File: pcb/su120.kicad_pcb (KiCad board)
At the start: 2 copper layers, 98.8 x 98 mm, 343 parts, among them J1 MJ-4PP-9, J2 Conn_01x03, J3 Conn_01x08, J4 Conn_01x08, J5 Conn_01x03, J6 MJ-4PP-9, J7 Conn_02x05_Odd_Even, J8 Conn_02x05_Odd_Even, SW1 SW_Push, SW10 SW_Push, SW11 SW_Push, SW12 SW_Push, SW13 SW_Push, SW14 SW_Push, SW15 SW_Push, SW16 SW_Push, SW17 SW_Push, SW18 SW_Push, SW19 Rotary_Encoder_Switch, SW2 SW_Push, SW20 Rotary_Encoder_Switch, SW21 SW_Push, SW3 SW_Push, SW4 SW_Push, SW5 SW_Push, SW6 SW_Push, SW7 SW_Push, SW8 SW_Push, SW9 SW_Push, U1 ProMicro

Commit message: first
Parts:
- removed the ? at (77.8, 59.5)
- removed the ? at (39.3, 150.4)
- removed the ? at (47.2, 150.4)
- removed the ? at (47.2, 142.1)
- removed the ? at (63.5, 135.7)
- removed the ? at (73.0, 135.7)
- removed the ? at (87.3, 135.7)
- removed the ? at (96.8, 135.7)
- removed the ? at (101.6, 135.7)
- removed the ? at (115.9, 135.7)
- removed the ? at (120.7, 135.7)
- removed the ? at (134.9, 135.7)
- removed the ? at (134.9, 150.0)
- removed the ? at (47.2, 145.7)
- removed the ? at (120.7, 150.0)
- removed the ? at (115.9, 150.0)
- removed the ? at (101.6, 150.0)
- removed the ? at (96.8, 150.0)
- removed the ? at (87.3, 150.0)
- removed the ? at (73.0, 150.0)
- removed the ? at (63.5, 150.0)
- removed the ? at (43.3, 142.1)
- removed the ? at (43.3, 135.3)
- removed the ? at (130.0, 55.2)
- removed the ? at (47.2, 135.3)
- removed the ? at (135.3, 55.2)
- removed the ? at (91.7, 55.2)
- removed the ? at (86.4, 55.2)
- removed the ? at (121.3, 55.2)
- removed the ? at (112.5, 55.2)
- removed the ? at (117.9, 55.2)
- removed the ? at (126.6, 55.2)
- removed the ? at (95.1, 55.2)
- removed the ? at (100.4, 55.2)
- removed the ? at (109.1, 55.2)
- removed the ? at (51.2, 142.1)
- removed the ? at (103.8, 55.2)
- removed the ? at (43.3, 150.4)
- removed the ? at (43.3, 145.7)
- removed the ? at (78.6, 66.7)
- removed the ? at (80.2, 59.5)
- removed the ? at (61.1, 152.4)
- removed the ? at (137.3, 57.2)
- removed the ? at (61.1, 133.3)
- removed the ? at (99.2, 152.4)
- removed the ? at (118.3, 152.4)
- removed the ? at (51.2, 145.7)
- removed the ? at (137.3, 152.4)
- removed the ? at (137.3, 133.3)
- removed the ? at (137.3, 114.3)
- removed the ? at (137.3, 95.2)
- removed the ? at (137.3, 76.2)
- removed the ? at (99.2, 76.2)
- removed the ? at (99.2, 133.4)
- removed the ? at (118.3, 133.4)
- removed the ? at (51.2, 135.3)
- removed the ? at (118.3, 76.2)
- removed the ? at (80.2, 73.8)
- removed the ? at (90.5, 143.3)
- removed the ? at (127.8, 142.9)
- removed the ? at (51.2, 150.4)
- removed the ? at (108.7, 142.9)
- removed the ? at (80.2, 142.9) (x2)
- removed the ? at (55.2, 142.1)
- removed the ? at (70.2, 143.3)
- removed the ? at (123.0, 66.7)
- removed the ? at (104.0, 66.7)
- removed the ? at (82.5, 59.5)
- removed the ? at (55.2, 145.7)
- removed the ? at (108.7, 63.5)
- removed the ? at (127.8, 63.5)
- removed the ? at (55.2, 135.3)
- removed the ? at (55.2, 150.4)
- removed the ? at (59.1, 135.4)
- removed the ? at (59.1, 150.4)
- removed the ? at (40.1, 80.2)
- removed the ? at (40.1, 75.4)
- removed the ? at (40.1, 84.9)
- removed the ? at (40.1, 70.6)
- removed the ? at (40.1, 88.5)
- removed the ? at (82.5, 73.8)
- removed the ? at (40.1, 98.0)
- removed the ? at (40.1, 102.8)
- removed the ? at (40.1, 93.3)
- removed the ? at (56.0, 55.2)
- removed the ? at (59.9, 55.2)
- removed the ? at (66.7, 55.2)
- removed the ? at (40.1, 106.4)
- removed the ? at (40.1, 111.1)
- removed the ? at (40.1, 120.7)
- removed the ? at (40.1, 115.9)
- removed the ? at (77.8, 73.8)
- removed the ? at (40.1, 131.4)
- removed the ? at (40.1, 124.2)
- removed the ? at (39.3, 142.5)
- removed the ? at (39.3, 135.3)
- removed the ? at (70.1, 55.2)
- removed the ? at (82.9, 55.2)
- removed the ? at (74.4, 55.2)
- removed the ? at (40.1, 58.5)
- removed the ? at (40.1, 67.1)
- removed the ? at (42.9, 55.2)
- removed the ? at (52.4, 55.2)
- removed the ? at (47.6, 55.2)
- removed the ? at (59.1, 141.8)
- removed the ? at (39.3, 145.7)
- removed D16, D17, D18, D19, D20: D, #footprint:diode_TH_SMD_rev2
- removed H133, H134, H135, H136, H137, H138, H139, H140, H210, H211, H212, H213, H41, H42, H43, H44, H45, H46, H47, H48, H49, H50, H57: MountingHole_Pad, #footprint:1pin_conn
- removed J1, J6: MJ-4PP-9, #footprint:MJ-4PP-9
- removed J2, J5: Conn_01x03, #footprint:StripLED_rev2
- removed J3, J4: Conn_01x08, #footprint:PinHeader_1x08_P2.54mm_Vertical_rev2
- removed J7, J8: Conn_02x05_Odd_Even, #footprint:IDC-Header_2x05_P2.54mm_Vertical
- removed JP1, JP2, JP3, JP4, JP5, JP6: SolderJumper_2_Open, #footprint:SolderJumper-2_P1.3mm_Open_Pad1.0x1.0mm
- removed SW16, SW17, SW21: SW_Push, #footprint:CherryMX_MidHeight_Choc_Hotswap_rev5
- removed SW18: SW_Push, #footprint:ResetSW
- removed SW19, SW20: Rotary_Encoder_Switch, #footprint:RotaryEncoder_Alps_EC11E-Switch_Vertical_H20mm_rev2
- removed U1: ProMicro, #footprint:ArduinoProMicro-ZigZag_rev5
- added ?: , #footprint:M1.4_tapping_Hole_rev2, F.Cu at (101.6, 40.5)
- added ?: , #footprint:M1.4_tapping_Hole_rev2, F.Cu at (120.7, 54.8)
- added ?: , #footprint:M1.4_tapping_Hole_rev2, F.Cu at (58.7, 54.8)
- added ?: , #footprint:M1.4_tapping_Hole_rev2, F.Cu at (134.9, 54.8)
- added ?: , #footprint:M1.4_tapping_Hole_rev2, F.Cu at (134.9, 40.5)
- added ?: , #footprint:M1.4_tapping_Hole_rev2, F.Cu at (96.8, 54.8)
- added ?: , #footprint:M1.4_tapping_Hole_rev2, F.Cu at (101.6, 54.8)
- added ?: , #footprint:M1.4_tapping_Hole_rev2, F.Cu at (58.7, 40.5)
- added ?: , #footprint:M2_Hole, F.Cu at (118.3, 76.2)
- added ?: , #footprint:M1.4_tapping_Hole_rev2, F.Cu at (44.5, 54.8)
- added ?: , #footprint:M2_Hole, F.Cu at (61.1, 57.2)
- added ?: , #footprint:M1.4_tapping_Hole_rev2, F.Cu at (77.8, 54.8)
- added ?: , #footprint:M1.4_tapping_Hole_rev2, F.Cu at (63.5, 73.8)
- added ?: , #footprint:M1.4_tapping_Hole_rev2, F.Cu at (77.8, 73.8)
- added ?: , #footprint:M1.4_tapping_Hole_rev2, F.Cu at (63.5, 54.8)
- added ?: , #footprint:M2_Hole, F.Cu at (61.1, 76.2)
- added ?: , #footprint:M1.4_tapping_Hole_rev2, F.Cu at (63.5, 40.5)
- added ?: , #footprint:M1.4_tapping_Hole_rev2, F.Cu at (82.5, 73.8)
- added ?: , #footprint:M2_Hole, F.Cu at (118.3, 57.2)
- added ?: , #footprint:M1.4_tapping_Hole_rev2, F.Cu at (115.9, 40.5)
- added ?: , #footprint:M1.4_tapping_Hole_rev2, F.Cu at (77.8, 59.5)
- added ?: , #footprint:M1.4_tapping_Hole_rev2, F.Cu at (63.5, 59.5)
- added ?: , #footprint:M2_Hole, F.Cu at (80.2, 57.2)
- added ?: , #footprint:M2_Hole, F.Cu at (99.2, 76.2)
- added ?: , #footprint:M1.4_tapping_Hole_rev2, F.Cu at (77.8, 40.5)
- added ?: , #footprint:M1.4_tapping_Hole_rev2, F.Cu at (58.7, 59.5)
- added ?: , #footprint:M2_Hole, F.Cu at (80.2, 76.2)
- added ?: , #footprint:M1.4_tapping_Hole_rev2, F.Cu at (58.7, 73.8)
- added ?: , #footprint:M2_Hole, F.Cu at (99.2, 57.2)
- added ?: , #footprint:CherryMX_MidHeight_Choc_Silk, F.Cu at (127.8, 66.7)
- added ?: , #footprint:M1.4_tapping_Hole_rev2, F.Cu at (44.5, 40.5)
- added ?: , #footprint:M1.4_tapping_Hole_rev2, F.Cu at (96.8, 40.5)
- added ?: , #footprint:M1.4_tapping_Hole_rev2, F.Cu at (82.5, 40.5)
- added ?: , #footprint:CherryMX_MidHeight_Choc_Silk, F.Cu at (108.7, 66.7)
- added ?: , #footprint:CherryMX_MidHeight_Choc_Silk, F.Cu at (89.7, 66.7)
- added ?: , #footprint:CherryMX_MidHeight_Choc_Silk, F.Cu at (70.6, 66.7)
- added ?: , #footprint:CherryMX_MidHeight_Choc_Silk, F.Cu at (51.6, 66.7)
- added ?: , #footprint:CherryMX_MidHeight_Choc_Silk, F.Cu at (51.6, 47.6)
- added ?: , #footprint:CherryMX_MidHeight_Choc_Silk, F.Cu at (70.6, 47.6)
- added ?: , #footprint:CherryMX_MidHeight_Choc_Silk, F.Cu at (89.7, 47.6)
- added ?: , #footprint:CherryMX_MidHeight_Choc_Silk, F.Cu at (127.8, 47.6)
- added ?: , #footprint:CherryMX_MidHeight_Choc_Silk, F.Cu at (108.7, 47.6)
- added ?: , #footprint:M1.4_tapping_Hole_rev2, F.Cu at (115.9, 54.8)
- added ?: , #footprint:M1.4_tapping_Hole_rev2, F.Cu at (120.7, 40.5)
- added ?: , #footprint:M1.4_tapping_Hole_rev2, F.Cu at (82.5, 54.8)
- added ?: , #footprint:M1.4_tapping_Hole_rev2, F.Cu at (82.5, 59.5)
- added D1: D, #footprint:diode_TH_SMD_rev2, F.Cu at (49.6, 39.7)
- added D10: D, #footprint:diode_TH_SMD_rev2, F.Cu at (125.8, 58.7)
- added D2: D, #footprint:diode_TH_SMD_rev2, F.Cu at (68.7, 39.7)
- added D3: D, #footprint:diode_TH_SMD_rev2, F.Cu at (87.7, 39.7)
- added D4: D, #footprint:diode_TH_SMD_rev2, F.Cu at (106.8, 39.7)
- added D5: D, #footprint:diode_TH_SMD_rev2, F.Cu at (125.8, 39.7)
- added D6: D, #footprint:diode_TH_SMD_rev2, F.Cu at (49.6, 58.7)
- added D7: D, #footprint:diode_TH_SMD_rev2, F.Cu at (68.7, 58.7)
- added D8: D, #footprint:diode_TH_SMD_rev2, F.Cu at (87.7, 58.7)
- added D9: D, #footprint:diode_TH_SMD_rev2, F.Cu at (106.8, 58.7)
- added H1: MountingHole_Pad, #footprint:1pin_conn, F.Cu at (47.2, 39.7)
- added H10: MountingHole_Pad, #footprint:1pin_conn, F.Cu at (123.4, 55.6)
- added H11: MountingHole_Pad, #footprint:1pin_conn, F.Cu at (43.7, 48.0)
- added H12: MountingHole_Pad, #footprint:1pin_conn, F.Cu at (59.5, 48.0)
- added H13: MountingHole_Pad, #footprint:1pin_conn, F.Cu at (62.7, 48.0)
- added H14: MountingHole_Pad, #footprint:1pin_conn, F.Cu at (78.6, 48.0)
- added H15: MountingHole_Pad, #footprint:1pin_conn, F.Cu at (81.8, 48.0)
- added H16: MountingHole_Pad, #footprint:1pin_conn, F.Cu at (97.6, 48.0)
- added H17: MountingHole_Pad, #footprint:1pin_conn, F.Cu at (100.8, 48.0)
- added H18: MountingHole_Pad, #footprint:1pin_conn, F.Cu at (116.7, 48.0)
- added H19: MountingHole_Pad, #footprint:1pin_conn, F.Cu at (119.9, 48.0)
- added H2: MountingHole_Pad, #footprint:1pin_conn, F.Cu at (66.3, 39.7)
- added H20: MountingHole_Pad, #footprint:1pin_conn, F.Cu at (135.7, 48.0)
- added H21: MountingHole_Pad, #footprint:1pin_conn, F.Cu at (47.2, 58.7)
- added H22: MountingHole_Pad, #footprint:1pin_conn, F.Cu at (66.3, 58.7)
- added H23: MountingHole_Pad, #footprint:1pin_conn, F.Cu at (85.3, 58.7)
- added H24: MountingHole_Pad, #footprint:1pin_conn, F.Cu at (104.4, 58.7)
- added H25: MountingHole_Pad, #footprint:1pin_conn, F.Cu at (123.4, 58.7)
- added H26: MountingHole_Pad, #footprint:1pin_conn, F.Cu at (47.2, 74.6)
- added H27: MountingHole_Pad, #footprint:1pin_conn, F.Cu at (66.3, 74.6)
- added H28: MountingHole_Pad, #footprint:1pin_conn, F.Cu at (85.3, 74.6)
- added H29: MountingHole_Pad, #footprint:1pin_conn, F.Cu at (104.4, 74.6)
- added H3: MountingHole_Pad, #footprint:1pin_conn, F.Cu at (85.3, 39.7)
- added H30: MountingHole_Pad, #footprint:1pin_conn, F.Cu at (123.4, 74.6)
- added H31: MountingHole_Pad, #footprint:1pin_conn, F.Cu at (43.7, 67.1)
- added H32: MountingHole_Pad, #footprint:1pin_conn, F.Cu at (59.5, 67.1)
- added H33: MountingHole_Pad, #footprint:1pin_conn, F.Cu at (62.7, 67.1)
- added H34: MountingHole_Pad, #footprint:1pin_conn, F.Cu at (78.6, 67.1)
- added H35: MountingHole_Pad, #footprint:1pin_conn, F.Cu at (81.8, 67.1)
- added H36: MountingHole_Pad, #footprint:1pin_conn, F.Cu at (97.6, 67.1)
- added H37: MountingHole_Pad, #footprint:1pin_conn, F.Cu at (100.8, 67.1)
- added H38: MountingHole_Pad, #footprint:1pin_conn, F.Cu at (116.7, 67.1)
- added H39: MountingHole_Pad, #footprint:1pin_conn, F.Cu at (119.9, 67.1)
- added H4: MountingHole_Pad, #footprint:1pin_conn, F.Cu at (104.4, 39.7)
- added H40: MountingHole_Pad, #footprint:1pin_conn, F.Cu at (135.7, 67.1)
- added H5: MountingHole_Pad, #footprint:1pin_conn, F.Cu at (123.4, 39.7)
- added H6: MountingHole_Pad, #footprint:1pin_conn, F.Cu at (47.2, 55.6)
- added H7: MountingHole_Pad, #footprint:1pin_conn, F.Cu at (66.3, 55.6)
- added H8: MountingHole_Pad, #footprint:1pin_conn, F.Cu at (85.3, 55.6)
- added H9: MountingHole_Pad, #footprint:1pin_conn, F.Cu at (104.4, 55.6)
- added SW1: SW_Push, #footprint:CherryMX_MidHeight_Choc_Hotswap_rev5, F.Cu at (51.6, 47.6)
- added SW10: SW_Push, #footprint:CherryMX_MidHeight_Choc_Hotswap_rev5, F.Cu at (127.8, 66.7)
- added SW2: SW_Push, #footprint:CherryMX_MidHeight_Choc_Hotswap_rev5, F.Cu at (70.6, 47.6)
- added SW3: SW_Push, #footprint:CherryMX_MidHeight_Choc_Hotswap_rev5, F.Cu at (89.7, 47.6)
- added SW4: SW_Push, #footprint:CherryMX_MidHeight_Choc_Hotswap_rev5, F.Cu at (108.7, 47.6)
- added SW5: SW_Push, #footprint:CherryMX_MidHeight_Choc_Hotswap_rev5, F.Cu at (127.8, 47.6)
- added SW6: SW_Push, #footprint:CherryMX_MidHeight_Choc_Hotswap_rev5, F.Cu at (51.6, 66.7)
- added SW7: SW_Push, #footprint:CherryMX_MidHeight_Choc_Hotswap_rev5, F.Cu at (70.6, 66.7)
- added SW8: SW_Push, #footprint:CherryMX_MidHeight_Choc_Hotswap_rev5, F.Cu at (89.7, 66.7)
- added SW9: SW_Push, #footprint:CherryMX_MidHeight_Choc_Hotswap_rev5, F.Cu at (108.7, 66.7)
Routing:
- net GND: track 1077.7 -> 0.00 mm, vias 131 -> 0
- net Y4: track 309.8 -> 0.00 mm, vias 7 -> 0
- net Y1: track 235.2 -> 417.2 mm, vias 2 -> 0
- net Y2: track 264.2 -> 417.2 mm, vias 2 -> 0
- net Y3: track 311.7 -> 209.0 mm, vias 6 -> 0
- net X8: track 95.2 -> 0.00 mm, vias 4 -> 0
- net Y6: track 88.6 -> 0.00 mm
- net X7: track 84.2 -> 0.00 mm, vias 3 -> 0
- net dummydata: track 77.3 -> 0.00 mm, vias 1 -> 0
- net X9: track 75.2 -> 0.00 mm, vias 2 -> 0
- net X10: track 73.8 -> 0.00 mm, vias 2 -> 0
- net X5: track 181.8 -> 115.3 mm, vias 1 -> 0
- net VCC: track 65.8 -> 0.00 mm, vias 2 -> 0
- net dummyVCC: track 57.0 -> 0.00 mm, vias 5 -> 0
- net data: track 56.5 -> 0.00 mm, vias 2 -> 0
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- removed copper zone on B.Cu, net GND
- removed copper zone on F.Cu, net GND
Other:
- board size 98.8 x 98 mm -> 94.1 x 94.1 mm
- board text removed: "0.25u"
- board text removed: "0.5u"
- board text removed: "0.75u"
- board text removed: "1.25u"
- board text removed: "1.5u"
- board text removed: "1/8u"
- board text removed: "1u"
- board text removed: "2u"
- board text removed: "3/8u"
- board text removed: "4"
- board text removed: "5"
- board text removed: "5/8u"
- board text removed: "6"
- board text removed: "A"
- board text removed: "B"
- board text removed: "B1"
- board text removed: "B2"
- board text removed: "B3"
- board text removed: "B4"
- board text removed: "B5"
- board text removed: "B6"
- board text removed: "C"
- board text removed: "C6"
- board text removed: "D"
- board text removed: "D0"
- board text removed: "D1"
- board text removed: "D4"
- board text removed: "D7"
- board text removed: "E"
- board text removed: "E6"
- board text removed: "F"
- board text removed: "F4"
- board text removed: "F5"
- board text removed: "F6"
- board text removed: "F7"
- board text removed: "G"
- board text removed: "GND"
- board text removed: "H"
- board text removed: "I"
- board text removed: "J"
- board text removed: "LED"
- board text removed: "LED Tape(back side)"
- board text removed: "RAW"
- board text removed: "RESET"
- board text removed: "RST"
- board text removed: "RX1"
- board text removed: "SU120 "YAKITORI" Rev.8 by @e3w2q"
- board text removed: "See back side printing"
- board text removed: "Solder back side jumper"
- board text removed: "TX0"
- board text removed: "VCC"
- board text removed: "for pin mapping"
- board text removed: "linear"
- board text removed: "stagger"

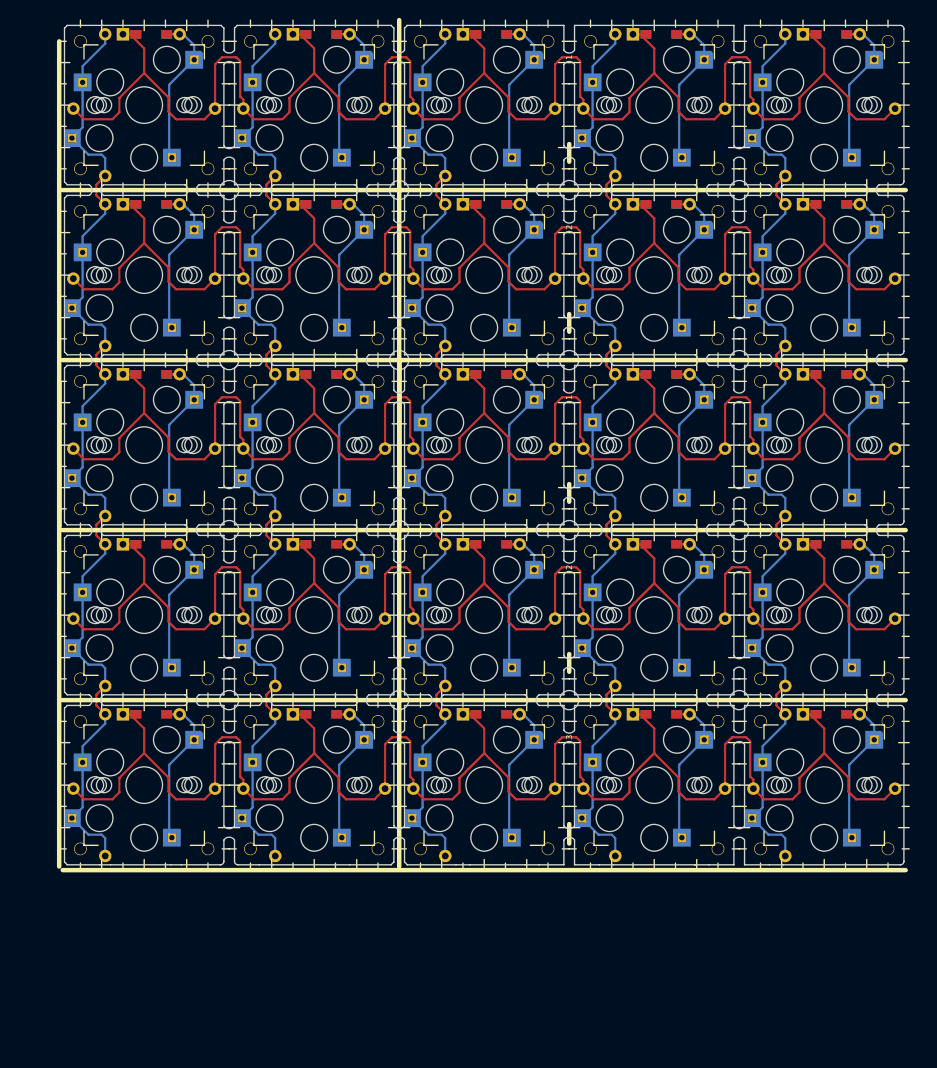
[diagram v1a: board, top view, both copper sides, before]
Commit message: modified center hole, changed diameter to 5.0mm
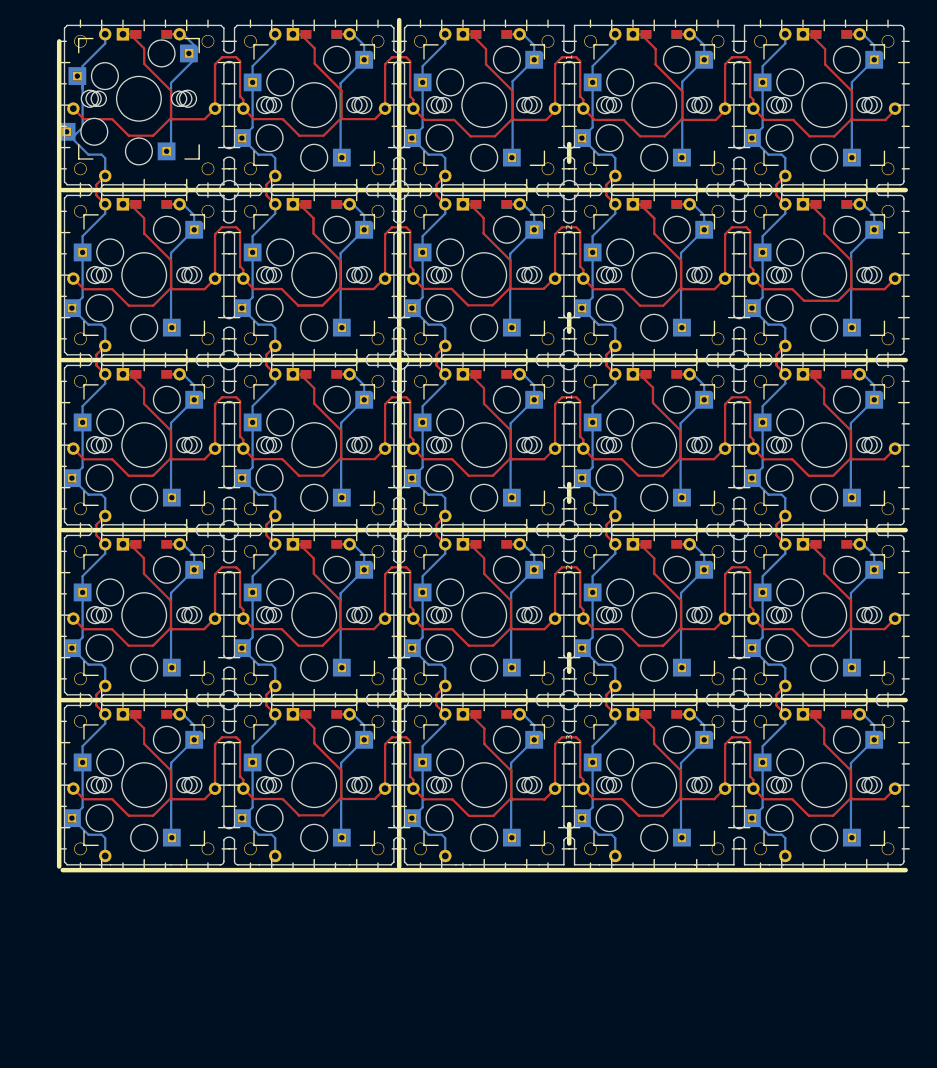
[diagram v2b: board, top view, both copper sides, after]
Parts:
- moved SW1 0.92 mm to (51.0, 46.9)
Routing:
- net Y2: track 417.2 -> 436.5 mm
- net Y1: track 417.2 -> 435.3 mm
- net Y3: track 209.0 -> 217.9 mm
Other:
- net class Default removed
- net class PWR removed
